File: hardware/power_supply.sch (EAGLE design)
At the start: 69 parts, among them Q1 BCX19SMD, Q2 BCX19SMD

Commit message: Updates 7-7
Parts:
- removed C10, C11, C12, C13, C14, C15, C16, C7, C8, C9: (no value), resistor:C-USC0402
- removed CD40109B: CD40109B, nixie_ticker:CD40109B
- removed R10, R11, R12, R13, R14, R17, R18, R7, R8, R9: (no value), resistor:R-US_R0805
- removed R15, R16, R19, R20, R21, R22, R23, R24: (no value), resistor:R-US_R0402
- removed U$10: 74AHC595, nixie_ticker:74AHC595
- removed U$11, U$15, U$19: IN14, nixie_ticker:IN14
- removed U$12, U$16, U$20: K155ID1, nixie_ticker:K155ID1
- removed U$13, U$14, U$18, U$21, U$22, U$23: TLP3873D, nixie_ticker:TLP3873D
- removed U$17, U$24: ZKFDS, nixie_ticker:ZKFDS
- removed U$25: UUR1C221MCL6GS, nixie_ticker:UUR1C221MCL6GS
- added D1: BAV21W, nixie_ticker:BAV21W
- added D2: MMBD914L, nixie_ticker:MMBD914L
- added JP2: (no value), pinhead:PINHD-2X3
- added L1: RLB9012, nixie_ticker:RLB9012
- added U1: MC34063, nixie_ticker:MC34063
- C1, C4, C5, C6: value (none) -> UUR1C221MCL6GS; device resistor:C-USC0402 -> nixie_ticker:UUR1C221MCL6GS
- Q1: value BCX19SMD -> IRF630N; device transistor-npn:BCX19SMD -> nixie_ticker:IRF630N
- Q2: value BCX19SMD -> (none); device transistor-npn:BCX19SMD -> transistor:BC807-16-PNP-SOT23-BEC
- R1, R2: value (none) -> 0.5; device resistor:R-US_R0805 -> resistor:R-US_R1206
- R3: value (none) -> 1k; device resistor:R-US_R0805 -> resistor:R-US_R0402
- R4: value (none) -> 13.7k; device resistor:R-US_R0805 -> resistor:R-US_R1206
- R5: value (none) -> 475k; device resistor:R-US_R0402 -> resistor:R-US_R1206
- R6: value (none) -> 4.02k; device resistor:R-US_R0402 -> resistor:R-US_R1206
- U$1: value IN14 -> EJ508A; device nixie_ticker:IN14 -> nixie_ticker:EJ508A
- U$2: value IN14 -> 3309P-1-202; device nixie_ticker:IN14 -> nixie_ticker:3309P-1-202
- U$3, U$4: value 74AHC595 -> T411001B; device nixie_ticker:74AHC595 -> nixie_ticker:T411001B
- U$5: value IN14 -> ZKFDS; device nixie_ticker:IN14 -> nixie_ticker:ZKFDS
- U$6: value K155ID1 -> ZKFDS; device nixie_ticker:K155ID1 -> nixie_ticker:ZKFDS
- U$7: value K155ID1 -> AP1507; device nixie_ticker:K155ID1 -> nixie_ticker:AP1507
- U$8: value K155ID1 -> B260A-13-F; device nixie_ticker:K155ID1 -> nixie_ticker:B260A-13-F
- U$9: value 74AHC595 -> RLB9013; device nixie_ticker:74AHC595 -> nixie_ticker:RLB9013
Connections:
- removed net DI_L: CD40109B.C, JP1.6
- removed net DS_1: CD40109B.G, R21.2, U$3.DS
- removed net N$100: U$15.9, U$16.9
- removed net N$101: U$10.Q2, U$16.I2
- removed net N$102: R1.2, U$13.E
- removed net N$103: R2.2, U$13.-
- removed net N$104: R13.1, U$19.A
- removed net N$105: R3.1, U$2.A
- removed net N$106: R3.2, U$14.E
- removed net N$107: R4.2, U$14.-
- removed net N$108: C2.1, R6.1, U$4.MR
- removed net N$109: C1.1, R5.1, U$3.MR
- removed net N$11: U$2.0, U$8.0
- removed net N$110: C3.1, R15.1, U$9.MR
- removed net N$111: C8.1, R16.1, U$10.MR
- removed net N$112: R7.2, U$18.E
- removed net N$113: R8.2, U$18.-
- removed net N$118: R7.1, U$5.A
- removed net N$119: R9.2, U$21.E
- removed net N$12: U$2.1, U$8.1
- removed net N$120: R10.2, U$21.-
- removed net N$121: U$19.0, U$20.0
- removed net N$122: U$19.1, U$20.1
- removed net N$123: U$19.2, U$20.2
- removed net N$124: U$19.3, U$20.3
- removed net N$125: U$19.4, U$20.4
- removed net N$126: U$19.5, U$20.5
- removed net N$127: U$19.6, U$20.6
- removed net N$128: U$19.7, U$20.7
- removed net N$129: U$19.8, U$20.8
- removed net N$13: U$2.2, U$8.2
- removed net N$130: U$19.9, U$20.9
- removed net N$14: U$2.3, U$8.3
- removed net N$145: R9.1, U$11.A
- removed net N$146: R11.2, U$22.E
- removed net N$147: R12.2, U$22.-
- removed net N$15: U$2.4, U$8.4
- removed net N$153: R13.2, U$23.E
- removed net N$154: R14.2, U$23.-
- removed net N$16: U$2.5, U$8.5
- removed net N$160: Q1.C, R18.1
- removed net N$161: Q2.C, R17.1
- removed net N$162: R17.2, U$11.PR
- removed net N$163: R18.2, U$2.PR
- removed net N$17: U$2.6, U$8.6
- removed net N$18: U$2.7, U$8.7
- removed net N$19: U$2.8, U$8.8
- removed net N$20: U$2.9, U$8.9
- removed net N$21: R23.2, U$4.Q7S, U$9.DS
- removed net N$22: R22.2, U$3.Q7S, U$4.DS
- removed net N$23: R24.2, U$10.DS, U$9.Q7S
- removed net N$24: U$3.Q2, U$7.I1
- removed net N$25: U$3.Q4, U$7.I2
- removed net N$26: U$3.Q5, U$7.I4
- removed net N$27: U$3.Q3, U$7.I8
- removed net N$28: U$13.+, U$3.Q1
- removed net N$29: U$3.Q0, U$8.I1
- removed net N$30: U$3.Q6, U$8.I2
- removed net N$31: U$5.0, U$6.0
- removed net N$32: U$5.1, U$6.1
- removed net N$33: U$5.2, U$6.2
- removed net N$34: U$5.3, U$6.3
- removed net N$35: U$5.4, U$6.4
- removed net N$36: U$5.5, U$6.5
- removed net N$37: U$5.6, U$6.6
- removed net N$38: U$5.7, U$6.7
- removed net N$39: U$5.8, U$6.8
- removed net N$40: U$5.9, U$6.9
- removed net N$41: U$3.Q7, U$8.I4
- removed net N$42: Q1.B, U$4.Q3
- removed net N$43: U$14.+, U$4.Q2
- removed net N$44: U$4.Q4, U$6.I1
- removed net N$45: U$4.Q6, U$6.I2
- removed net N$46: U$4.Q7, U$6.I4
- removed net N$47: U$4.Q0, U$8.I8
- removed net N$48: U$4.Q5, U$6.I8
- removed net N$49: U$18.+, U$4.Q1
- removed net N$50: U$12.I1, U$9.Q3
- removed net N$51: U$12.I2, U$9.Q4
- removed net N$52: U$12.I4, U$9.Q5
- removed net N$53: U$12.I8, U$9.Q0
- removed net N$54: U$16.I1, U$9.Q7
- removed net N$55: Q2.B, U$9.Q2
- removed net N$56: U$21.+, U$9.Q1
- removed net N$57: R1.1, U$1.A
- removed net N$58: U$10.Q3, U$16.I4
- removed net N$59: U$16.I8, U$9.Q6
- removed net N$60: U$10.Q0, U$22.+
- removed net N$61: U$11.0, U$12.0
- removed net N$62: U$11.1, U$12.1
- removed net N$63: U$11.2, U$12.2
- removed net N$64: U$11.3, U$12.3
- removed net N$65: U$11.4, U$12.4
- removed net N$66: U$11.5, U$12.5
- removed net N$67: U$11.6, U$12.6
- removed net N$68: U$11.7, U$12.7
- removed net N$69: U$11.8, U$12.8
- removed net N$70: U$11.9, U$12.9
- removed net N$81: U$10.Q4, U$20.I1
- removed net N$82: U$10.Q6, U$20.I2
- removed net N$83: U$10.Q7, U$20.I4
- removed net N$84: U$10.Q5, U$20.I8
- removed net N$85: U$10.Q1, U$23.+
- removed net N$90: R11.1, U$15.A
- removed net N$91: U$15.0, U$16.0
- removed net N$92: U$15.1, U$16.1
- removed net N$93: U$15.2, U$16.2
- removed net N$94: U$15.3, U$16.3
- removed net N$95: U$15.4, U$16.4
- removed net N$96: U$15.5, U$16.5
- removed net N$97: U$15.6, U$16.6
- removed net N$98: U$15.7, U$16.7
- removed net N$99: U$15.8, U$16.8
- removed net SHCP_5V: CD40109B.F, R19.2, U$10.SHCP, U$3.SHCP, U$4.SHCP, U$9.SHCP
- removed net SHCP_L: CD40109B.B, JP1.5
- removed net STCP_5V: CD40109B.E, R20.2, U$10.STCP, U$3.STCP, U$4.STCP, U$9.STCP
- removed net STCP_L: CD40109B.A, JP1.4
- new net +12V: C5.+, U$1.P$1, U$3.1, U$4.2
- new net DI: JP1.6, JP2.2
- new net SHCP: JP1.5, JP2.1
- new net STCP: JP1.4, JP2.3
- net +3V3: now also JP2.5; no longer C16.1, CD40109B.EN, CD40109B.VCC
- net +5V: now also C6.+, JP2.6, U$7.FB, U$9.2; no longer C10.1, C11.1, C12.1, C13.1, C14.1, C15.1, C4.1, C5.1, C6.1, C7.1, C9.1, CD40109B.VDD, R15.2, R16.2, R5.2, R6.2, U$10.VCC, U$12.VCC, U$16.VCC, U$20.VCC, U$25.+, U$3.VCC, U$4.VCC, U$6.VCC, U$7.VCC, U$8.VCC, U$9.VCC
- net GND: now also C1.-, C4.-, C5.-, C6.-, JP2.4, Q1.S, Q2.C, R3.1, U$1.P$2, U$1.P$3, U$2.P$3, U$6.P$1, U$7.SD, U$8.A, U1.GND; no longer C1.2, C10.2, C11.2, C12.2, C13.2, C14.2, C15.2, C16.2, C4.2, C5.2, C6.2, C7.2, C8.2, C9.2, CD40109B.VSS, Q1.E, Q2.E, R10.1, R12.1, R14.1, R19.1, R2.1, R20.1, R21.1, R22.1, R23.1, R24.1, R8.1, U$10.GND, U$10.OE, U$12.GND, U$16.GND, U$20.GND, U$24.P$1, U$25.-, U$3.GND, U$3.OE, U$4.GND, U$4.OE, U$6.GND, U$8.GND, U$9.GND, U$9.OE
- net N$1: now also C1.+, L1.1, R1.2, R2.2, U1.CD, U1.CS, U1.IS; no longer U$1.0, U$7.0
- net N$10: now also U$7.OUT, U$8.C, U$9.1; no longer U$1.9, U$7.9
- net N$2: now also D1.A, L1.2, Q1.D; no longer U$1.1, U$7.1
- net N$3: now also R6.1, U$2.P$2; no longer U$1.2, U$7.2
- net N$4: now also D2.A, Q2.B, R3.2, U1.ES; no longer U$1.3, U$7.3
- net N$5: now also D2.C, Q1.G, Q2.E; no longer U$1.4, U$7.4
- net N$6: now also R1.1, R2.1, U$3.2, U1.V+; no longer U$1.5, U$7.5
- net N$7: now also C2.1, U1.CT; no longer U$1.6, U$7.6
- net N$8: now also U$4.1, U$7.VIN; no longer U$1.7, U$7.7
- net N$9: now also C3.1, R4.2, R5.1, R6.2, U1.FB; no longer U$1.8, U$7.8
- net V+: now also C4.+, D1.C, R5.2, U$5.P$1; no longer U$13.C, U$14.C, U$17.P$1, U$18.C, U$21.C, U$22.C, U$23.C
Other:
- moved on the sheet: C2, C3, JP1, R1, R2, R3, R4, R5, R6

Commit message: Updating power supply 7/10
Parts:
- renumbered U$7 to U2, U$8 to D3
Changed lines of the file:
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@@
 <part name="P+4" library="supply1" library_urn="urn:adsk.eagle:library:371" deviceset="V+" device=""/>
 <part name="GND12" library="supply1" library_urn="urn:adsk.eagle:library:371" deviceset="GND" device=""/>
-<part name="U$7" library="nixie_ticker" library_urn="urn:adsk.eagle:library:3857935" deviceset="AP1507" device="" package3d_urn="urn:adsk.eagle:package:4010820/1"/>
+<part name="U2" library="nixie_ticker" library_urn="urn:adsk.eagle:library:3857935" deviceset="AP1507" device="" package3d_urn="urn:adsk.eagle:package:4010820/1"/>
 <part name="P+5" library="supply1" library_urn="urn:adsk.eagle:library:371" deviceset="+12V" device=""/>
 <part name="C5" library="nixie_ticker" library_urn="urn:adsk.eagle:library:3857935" deviceset="UUR1C221MCL6GS" device="" package3d_urn="urn:adsk.eagle:package:3945414/1"/>
-<part name="U$8" library="nixie_ticker" library_urn="urn:adsk.eagle:library:3857935" deviceset="B260A-13-F" device="" package3d_urn="urn:adsk.eagle:package:4010839/1"/>
+<part name="D3" library="nixie_ticker" library_urn="urn:adsk.eagle:library:3857935" deviceset="B260A-13-F" device="" package3d_urn="urn:adsk.eagle:package:4010839/1"/>
 <part name="GND13" library="supply1" library_urn="urn:adsk.eagle:library:371" deviceset="GND" device=""/>
 <part name="U$9" library="nixie_ticker" library_urn="urn:adsk.eagle:library:3857935" deviceset="RLB9013" device="" package3d_urn="urn:adsk.eagle:package:4010895/3"/>
@@
 <instance part="P+4" gate="1" x="96.52" y="63.5" rot="R270"/>
 <instance part="GND12" gate="1" x="96.52" y="58.42" rot="R90"/>
-<instance part="U$7" gate="G$1" x="121.92" y="38.1"/>
+<instance part="U2" gate="G$1" x="121.92" y="38.1"/>
 <instance part="P+5" gate="1" x="96.52" y="35.56" rot="R90"/>
 <instance part="C5" gate="G$1" x="30.48" y="78.74"/>
-<instance part="U$8" gate="G$1" x="137.16" y="33.02" rot="R90"/>
+<instance part="D3" gate="G$1" x="137.16" y="33.02" rot="R90"/>
 <instance part="GND13" gate="1" x="121.92" y="22.86"/>
 <instance part="U$9" gate="G$1" x="142.24" y="38.1"/>
@@
 </segment>
 <segment>
-<pinref part="U$7" gate="G$1" pin="GND"/>
-<pinref part="U$8" gate="G$1" pin="A"/>
+<pinref part="U2" gate="G$1" pin="GND"/>
+<pinref part="D3" gate="G$1" pin="A"/>
 <wire x1="137.16" y1="30.48" x2="137.16" y2="25.4" width="0.1524" layer="91"/>
 <wire x1="137.16" y1="25.4" x2="127" y2="25.4" width="0.1524" layer="91"/>
-<pinref part="U$7" gate="G$1" pin="SD"/>
+<pinref part="U2" gate="G$1" pin="SD"/>
 <wire x1="116.84" y1="25.4" x2="121.92" y2="25.4" width="0.1524" layer="91"/>
 <pinref part="GND13" gate="1" pin="GND"/>
@@
 <net name="N$10" class="0">
 <segment>
-<pinref part="U$7" gate="G$1" pin="OUT"/>
+<pinref part="U2" gate="G$1" pin="OUT"/>
 <wire x1="134.62" y1="38.1" x2="137.16" y2="38.1" width="0.1524" layer="91"/>
 <pinref part="U$9" gate="G$1" pin="1"/>
-<pinref part="U$8" gate="G$1" pin="C"/>
+<pinref part="D3" gate="G$1" pin="C"/>
 <wire x1="137.16" y1="35.56" x2="137.16" y2="38.1" width="0.1524" layer="91"/>
 </segment>
@@
 <net name="N$8" class="0">
 <segment>
-<pinref part="U$7" gate="G$1" pin="VIN"/>
+<pinref part="U2" gate="G$1" pin="VIN"/>
 <pinref part="U$4" gate="G$1" pin="1"/>
 </segment>
@@
 <wire x1="149.86" y1="50.8" x2="149.86" y2="38.1" width="0.1524" layer="91"/>
 <wire x1="149.86" y1="38.1" x2="149.86" y2="33.02" width="0.1524" layer="91"/>
-<pinref part="U$7" gate="G$1" pin="FB"/>
+<pinref part="U2" gate="G$1" pin="FB"/>
 <wire x1="121.92" y1="50.8" x2="149.86" y2="50.8" width="0.1524" layer="91"/>
 </segment>

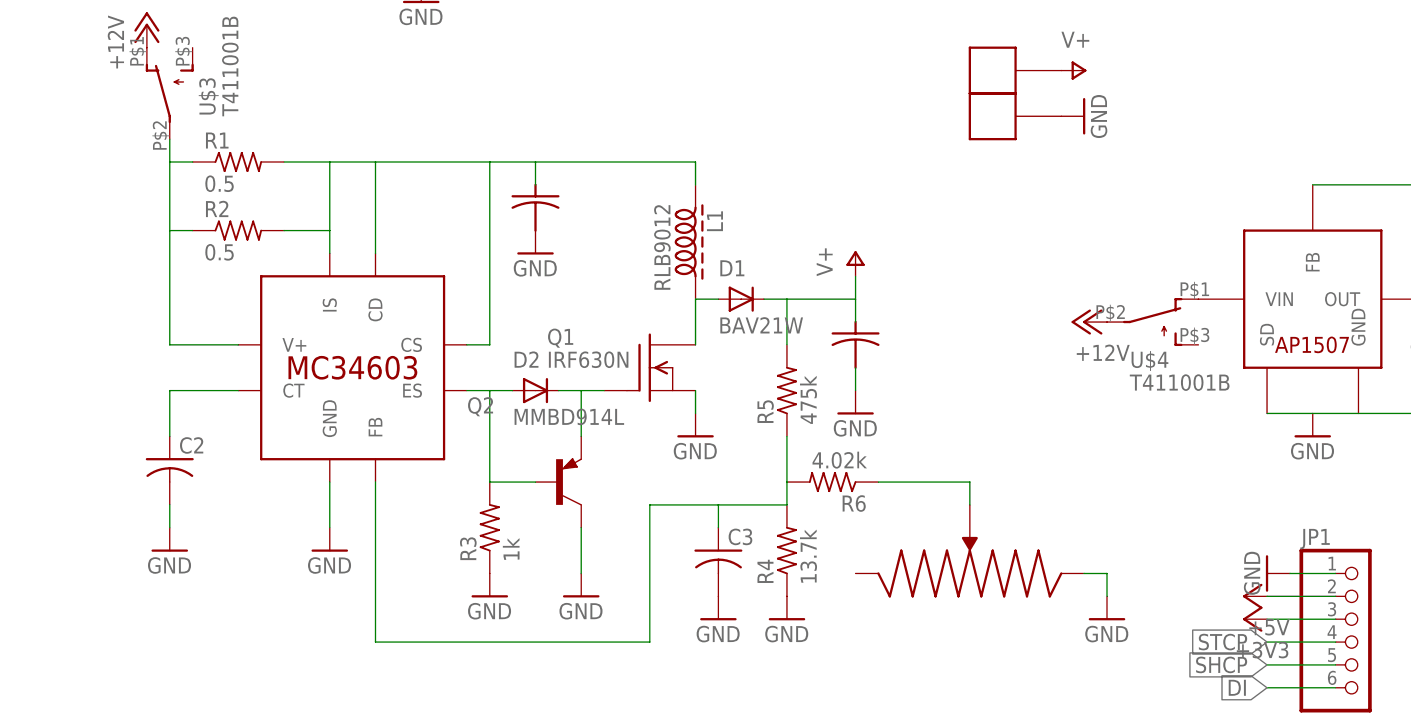
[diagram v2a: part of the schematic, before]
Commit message: Updating power_supply, 7-11
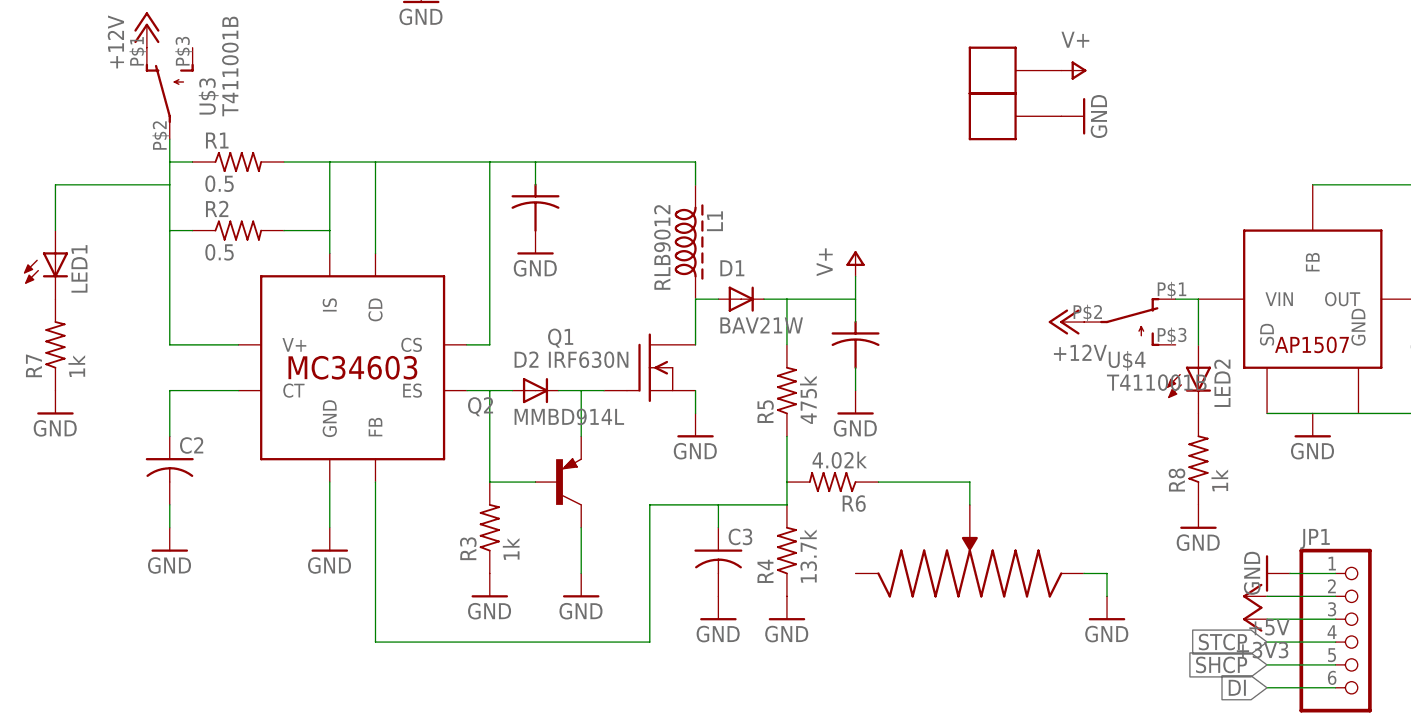
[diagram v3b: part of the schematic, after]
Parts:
- added LED1, LED2: (no value), led:LEDSML0805
- added R7, R8: 1k, resistor:R-US_R0402
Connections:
- new net N$11: LED1.C, R7.2
- new net N$12: LED2.C, R8.2
- net GND: now also R7.1, R8.1
- net N$6: now also LED1.A
- net N$8: now also LED2.A
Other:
- moved on the sheet: U$4
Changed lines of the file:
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@@
 <part name="+3V1" library="supply1" library_urn="urn:adsk.eagle:library:371" deviceset="+3V3" device=""/>
 <part name="+3V2" library="supply1" library_urn="urn:adsk.eagle:library:371" deviceset="+3V3" device=""/>
+<part name="LED1" library="led" library_urn="urn:adsk.eagle:library:259" deviceset="LED" device="SML0805" package3d_urn="urn:adsk.eagle:package:15830/1"/>
+<part name="LED2" library="led" library_urn="urn:adsk.eagle:library:259" deviceset="LED" device="SML0805" package3d_urn="urn:adsk.eagle:package:15830/1"/>
+<part name="R7" library="resistor" library_urn="urn:adsk.eagle:library:348" deviceset="R-US_" device="R0402" package3d_urn="urn:adsk.eagle:package:26058/1" value="1k"/>
+<part name="GND16" library="supply1" library_urn="urn:adsk.eagle:library:371" deviceset="GND" device=""/>
+<part name="R8" library="resistor" library_urn="urn:adsk.eagle:library:348" deviceset="R-US_" device="R0402" package3d_urn="urn:adsk.eagle:package:26058/1" value="1k"/>
+<part name="GND17" library="supply1" library_urn="urn:adsk.eagle:library:371" deviceset="GND" device=""/>
 </parts>
 <sheets>
@@
 <instance part="GND11" gate="1" x="22.86" y="71.12"/>
 <instance part="U$3" gate="G$1" x="-5.08" y="60.96"/>
-<instance part="U$4" gate="G$1" x="104.14" y="35.56" rot="R270"/>
+<instance part="U$4" gate="G$1" x="101.6" y="35.56" rot="R270"/>
 <instance part="U$5" gate="G$1" x="86.36" y="63.5"/>
 <instance part="U$6" gate="G$1" x="86.36" y="58.42"/>
@@
 <instance part="GND12" gate="1" x="96.52" y="58.42" rot="R90"/>
 <instance part="U2" gate="G$1" x="121.92" y="38.1"/>
-<instance part="P+5" gate="1" x="96.52" y="35.56" rot="R90"/>
+<instance part="P+5" gate="1" x="93.98" y="35.56" rot="R90"/>
 <instance part="C5" gate="G$1" x="30.48" y="78.74"/>
 <instance part="D3" gate="G$1" x="137.16" y="33.02" rot="R90"/>
@@
 <instance part="+3V1" gate="G$1" x="144.78" y="0" rot="R90"/>
 <instance part="+3V2" gate="G$1" x="114.3" y="2.54" rot="R90"/>
+<instance part="LED1" gate="G$1" x="-17.78" y="43.18"/>
+<instance part="LED2" gate="G$1" x="109.22" y="30.48"/>
+<instance part="R7" gate="G$1" x="-17.78" y="33.02" rot="R90"/>
+<instance part="GND16" gate="1" x="-17.78" y="25.4"/>
+<instance part="R8" gate="G$1" x="109.22" y="20.32" rot="R90"/>
+<instance part="GND17" gate="1" x="109.22" y="12.7"/>
 </instances>
 <busses>
@@
 <pinref part="GND15" gate="1" pin="GND"/>
 </segment>
+<segment>
+<pinref part="R7" gate="G$1" pin="1"/>
+<pinref part="GND16" gate="1" pin="GND"/>
+</segment>
+<segment>
+<pinref part="R8" gate="G$1" pin="1"/>
+<pinref part="GND17" gate="1" pin="GND"/>
+</segment>
 </net>
 <net name="N$2" class="0">
@@
 <wire x1="-5.08" y1="45.72" x2="-2.54" y2="45.72" width="0.1524" layer="91"/>
 <pinref part="R1" gate="G$1" pin="1"/>
-<wire x1="-5.08" y1="45.72" x2="-5.08" y2="53.34" width="0.1524" layer="91"/>
+<wire x1="-5.08" y1="45.72" x2="-5.08" y2="50.8" width="0.1524" layer="91"/>
+<wire x1="-5.08" y1="50.8" x2="-5.08" y2="53.34" width="0.1524" layer="91"/>
 <wire x1="-5.08" y1="53.34" x2="-2.54" y2="53.34" width="0.1524" layer="91"/>
 <wire x1="-5.08" y1="55.88" x2="-5.08" y2="53.34" width="0.1524" layer="91"/>
 <pinref part="U$3" gate="G$1" pin="2"/>
+<pinref part="LED1" gate="G$1" pin="A"/>
+<wire x1="-17.78" y1="45.72" x2="-17.78" y2="50.8" width="0.1524" layer="91"/>
+<wire x1="-17.78" y1="50.8" x2="-5.08" y2="50.8" width="0.1524" layer="91"/>
 </segment>
 </net>
@@
 <pinref part="U2" gate="G$1" pin="VIN"/>
 <pinref part="U$4" gate="G$1" pin="1"/>
+<wire x1="106.68" y1="38.1" x2="109.22" y2="38.1" width="0.1524" layer="91"/>
+<pinref part="LED2" gate="G$1" pin="A"/>
+<wire x1="109.22" y1="33.02" x2="109.22" y2="38.1" width="0.1524" layer="91"/>
 </segment>
 </net>
@@
 </segment>
 </net>
+<net name="N$11" class="0">
+<segment>
+<pinref part="LED1" gate="G$1" pin="C"/>
+<pinref part="R7" gate="G$1" pin="2"/>
+</segment>
+</net>
+<net name="N$12" class="0">
+<segment>
+<pinref part="LED2" gate="G$1" pin="C"/>
+<pinref part="R8" gate="G$1" pin="2"/>
+</segment>
+</net>
